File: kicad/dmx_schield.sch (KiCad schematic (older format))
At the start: 103 parts, among them J1 Conn_01x17, J2 Conn_01x17, J250 Conn_01x01, J251 Conn_01x01, J30 Conn_01x04, J40 Conn_01x06, J41 Conn_01x01, J42 Conn_01x01, J43 Conn_01x01, J50 Conn_01x02, J60 Conn_01x03, Q1 BSR14, Q50 IRLML5203, SW1 SW_Push, SW2 SW_Push, SW3 SW_Push, SW4 SW_Push, U1 DCDC-SIP8-1-2-(3)-6-7, U11 DCDC-SIP7-1-2-4-6, U140 LM317_3PinPackage, U3 LTV-847S, U5 LTV-827S, U6 ADUM1301, U60 MAX481E, U61 74LVC2G34, U7 REE-0505S/1S7E_0505S1.5UP

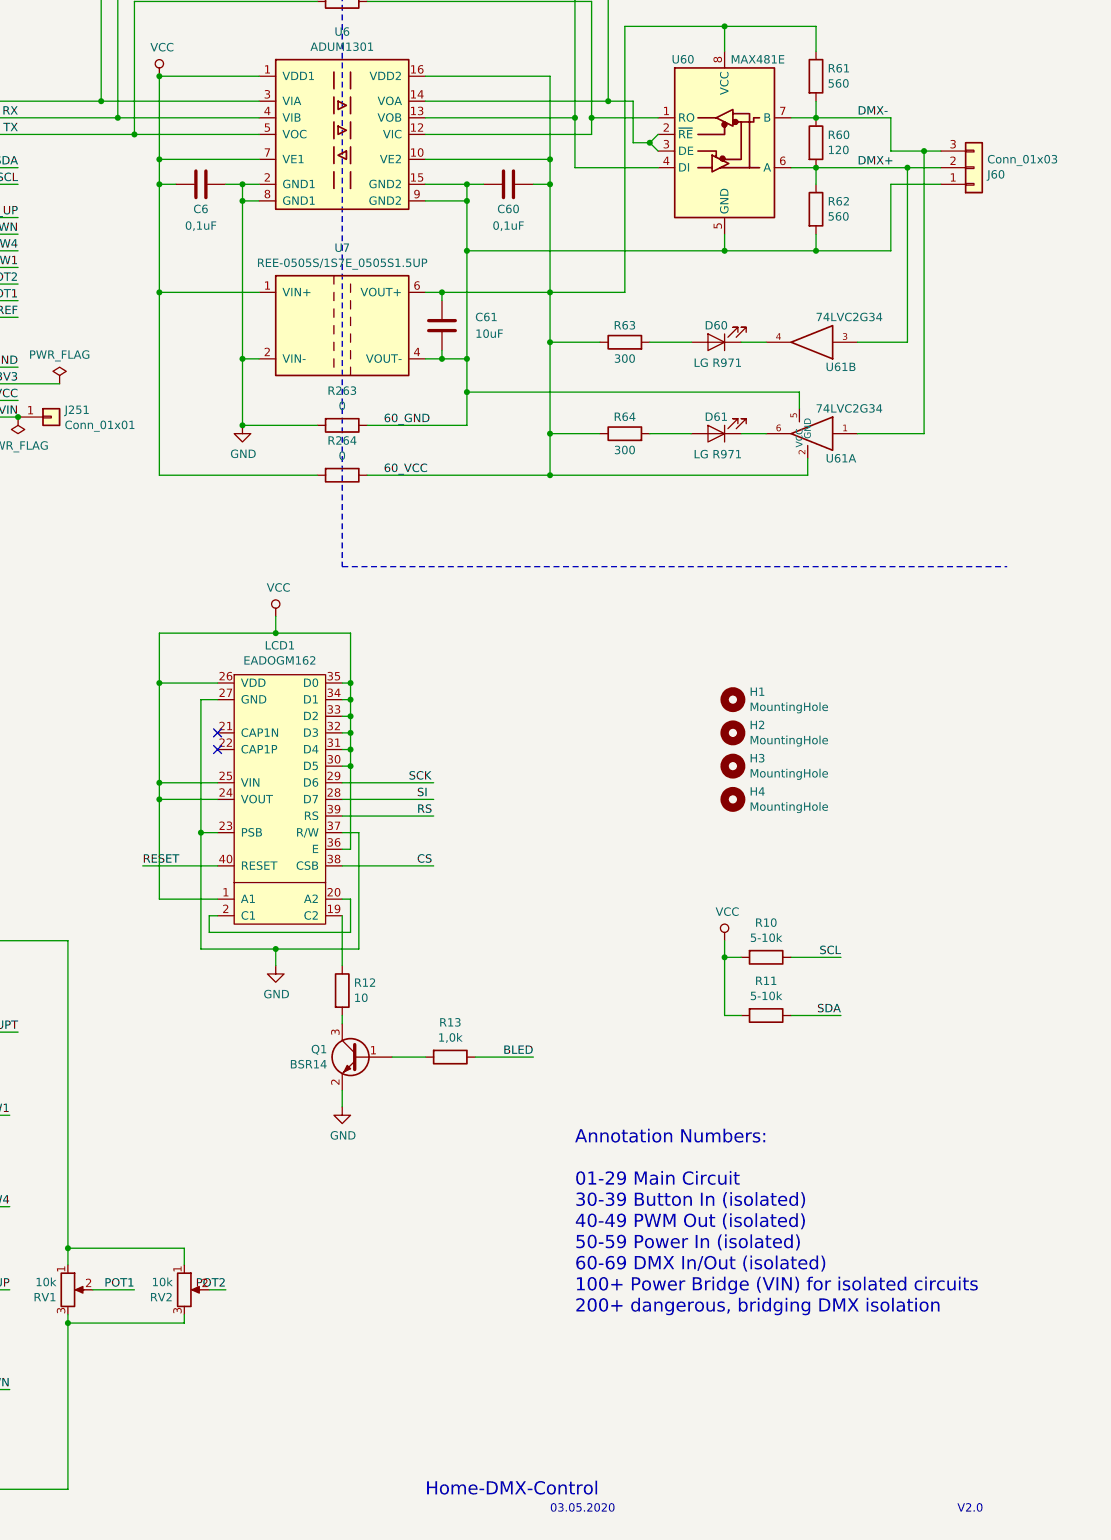
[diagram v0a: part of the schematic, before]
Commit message: fixed routing errors and error in library
tested is everything, but the DMX circuit and LDO
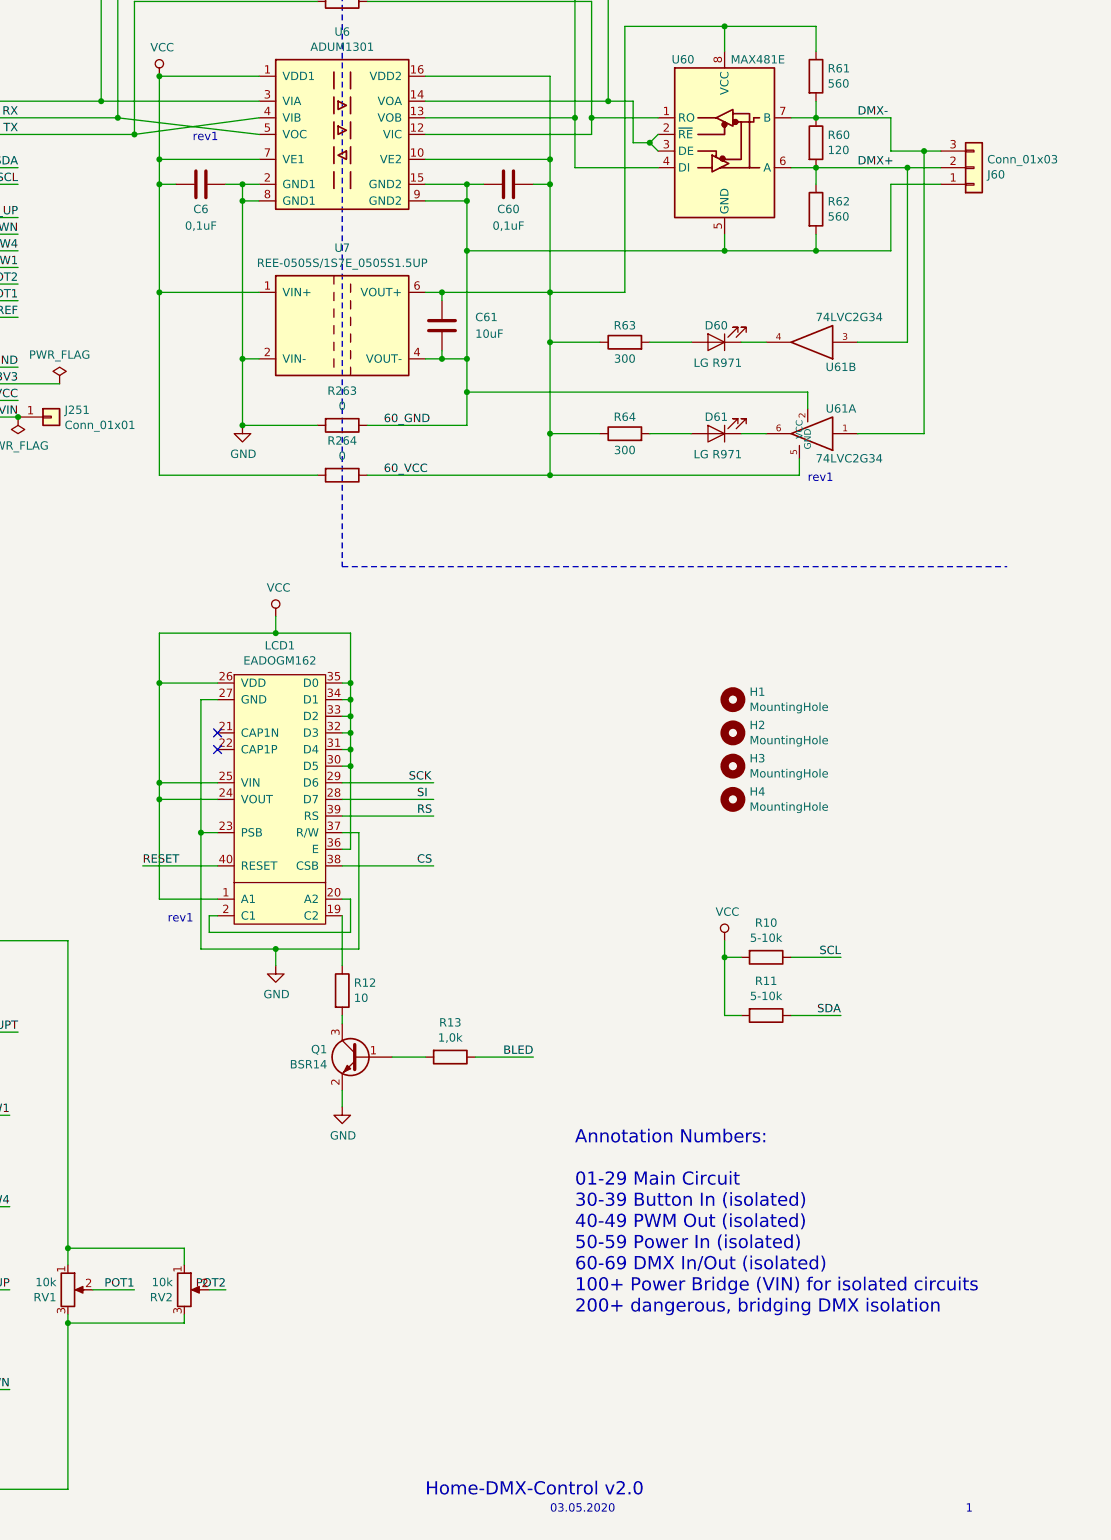
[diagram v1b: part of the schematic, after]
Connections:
- net 60_GND: now also U61.2 (GND); no longer U61.5 (VCC)
- net 60_VCC: now also U61.5 (VCC); no longer U61.2 (GND)
- net RX: now also U6.5 (VOC); no longer U6.4 (VIB)
- net TX: now also U6.4 (VIB); no longer U6.5 (VOC)
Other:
- note added: "1"
- note added: "Home-DMX-Control v2.0"
- note added: "rev1"
- note removed: "Home-DMX-Control"
- note removed: "V2.0"
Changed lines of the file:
@@
 F 3 "http://www.ti.com/lit/sg/scyt129e/scyt129e.pdf" H 14500 4550 50  0001 C CNN
 	1    14500 4550
-	-1   0    0    -1
+	-1   0    0    1
 $EndComp
 $Comp
@@
 Text Notes 12950 11050 0    50   ~ 0
 03.05.2020
-Text Notes 15400 11050 0    50   ~ 0
-V2.0
+Text Notes 15450 11050 0    50   ~ 0
+1
 Wire Wire Line
 	6750 3850 6350 3850
@@
 Wire Wire Line
 	11550 1950 10450 1950
-Connection ~ 10350 2650
 $Comp
 L my_lib:ADUM1301 U6
@@
 Wire Wire Line
 	10450 2750 10450 1950
-Connection ~ 10450 2750
 Wire Wire Line
 	10600 2400 10600 2900
@@
 	3450 6700 3500 6700
 Wire Wire Line
-	14100 4550 14250 4550
-Wire Wire Line
-	14500 4700 14500 4800
-Wire Wire Line
-	14500 4800 12950 4800
+	14450 4700 14450 4800
+Wire Wire Line
+	14450 4800 12950 4800
 Connection ~ 12950 4800
 Wire Wire Line
@@
 	12950 4550 12950 4800
 Wire Wire Line
-	14450 4400 14450 4300
-Wire Wire Line
-	14450 4300 12450 4300
+	14500 4400 14500 4300
+Wire Wire Line
+	14500 4300 12450 4300
 Connection ~ 12450 4300
 Wire Wire Line
@@
 RX
 Wire Wire Line
-	10350 2650 11200 2650
-Wire Wire Line
-	10450 2750 11200 2750
-Wire Wire Line
 	11700 7350 11750 7350
 Wire Wire Line
@@
 	4750 6750 4750 6700
 Text Notes 12200 10950 0    79   ~ 0
-Home-DMX-Control
+Home-DMX-Control v2.0
+Wire Wire Line
+	14100 4550 14250 4550
+Wire Wire Line
+	10450 2750 11200 2650
+Connection ~ 10450 2750
+Wire Wire Line
+	10350 2650 11200 2750
+Connection ~ 10350 2650
+Text Notes 14500 4850 0    50   ~ 0
+rev1
+Text Notes 10800 2800 0    50   ~ 0
+rev1
+Text Notes 10650 7500 0    50   ~ 0
+rev1
 $EndSCHEMATC
